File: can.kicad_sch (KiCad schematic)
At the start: 7 parts, among them U2 MCP2517FD-xJHA, U6 MCP2542FDxMF, Y1 40MHz

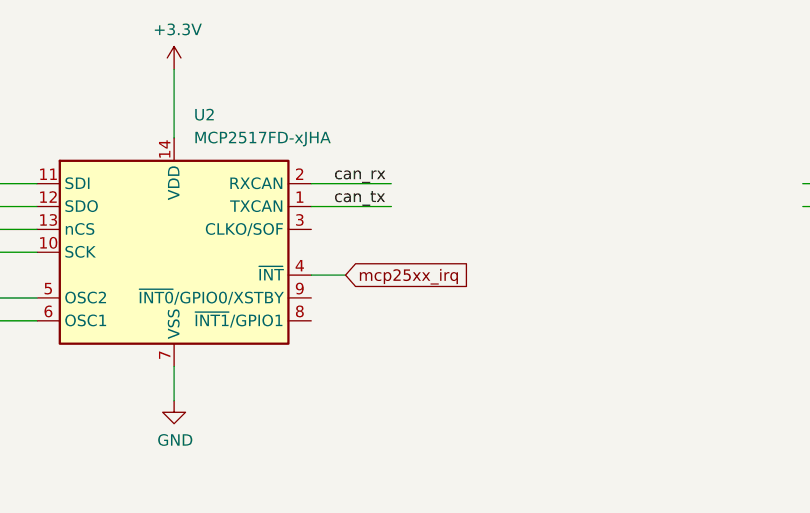
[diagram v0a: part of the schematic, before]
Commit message: move to 4 layers
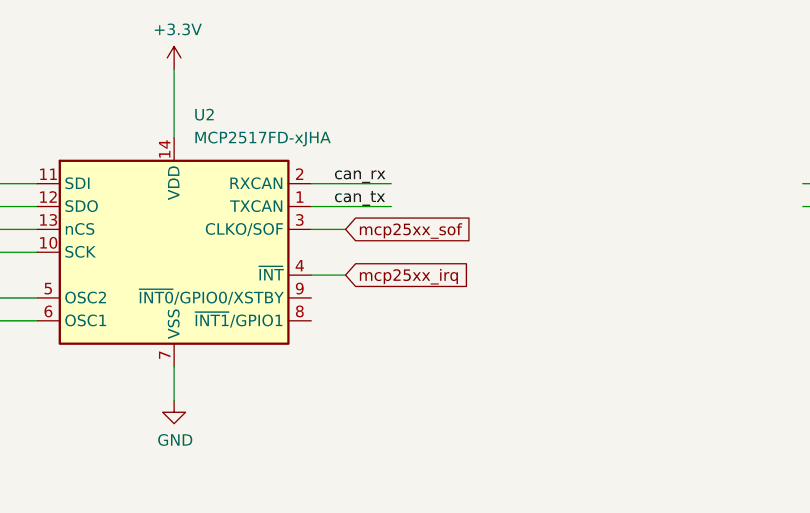
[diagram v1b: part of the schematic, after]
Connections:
- net mcp25xx_sof: now reaches U2.3 (CLKO/SOF)
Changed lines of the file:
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@@
+    (stroke (width 0) (type default))
+  )
+  (wire (pts (xy 123.19 68.58) (xy 127 68.58))
     (stroke (width 0) (type default))
   )
@@
       (effects (font (size 1.27 1.27)) hide)
     )
+  )
+  (global_label "mcp25xx_sof" (shape input) (at 127 68.58 0)
+    (effects (font (size 1.27 1.27)) (justify left))
+    (property "Intersheetrefs" "${INTERSHEET_REFS}" (at 127 68.58 0)
+      (effects (font (size 1.27 1.27)) hide)
+    )

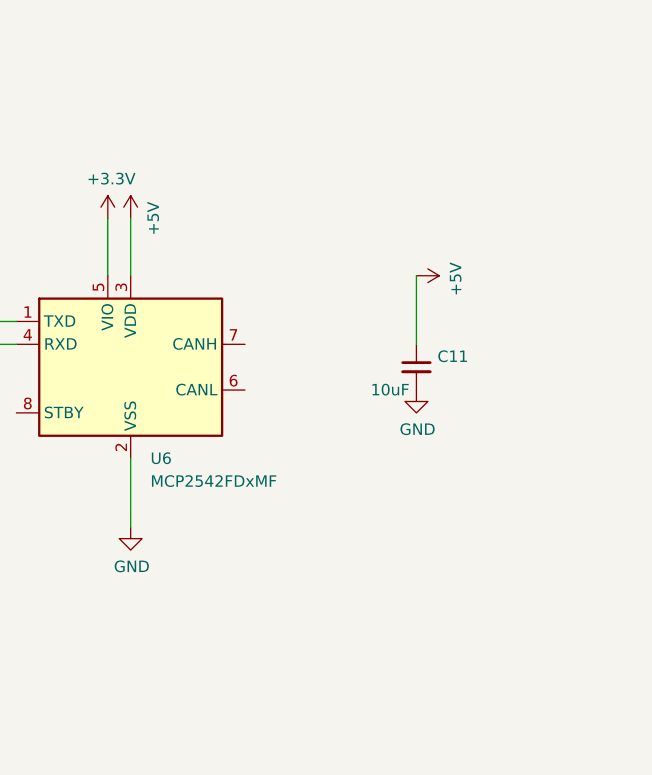
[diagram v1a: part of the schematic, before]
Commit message: Add CAN TVS protection
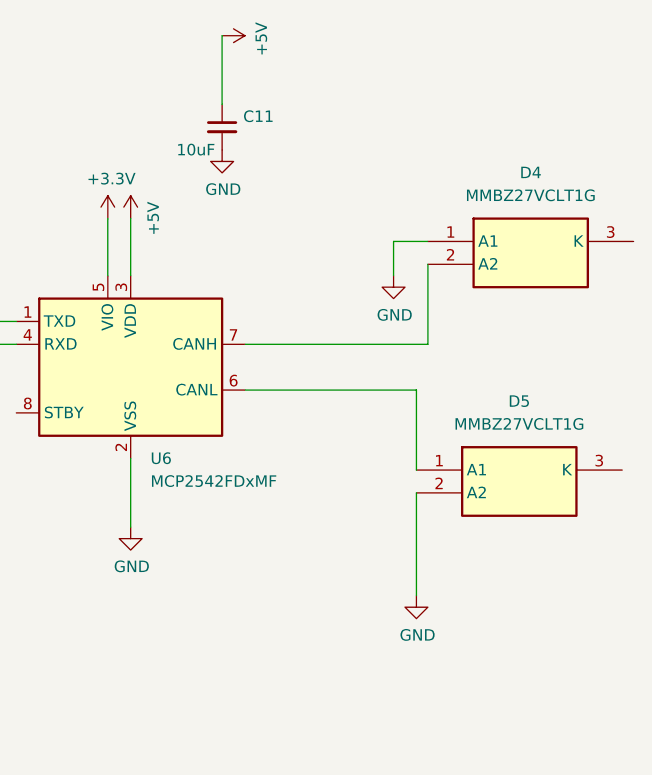
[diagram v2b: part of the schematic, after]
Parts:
- added D4, D5: MMBZ27VCLT1G, LTP-305G:SOT96P237X111-3N, symbol MMBZ27VCLT1G:MMBZ27VCLT1G
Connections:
- net GND: now also D4.1 (A1), D5.2 (A2)
- net at U6.6 (CANL): now also D5.1 (A1)
- net at U6.7 (CANH): now also D4.2 (A2)
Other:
- moved on the sheet: C11

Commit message: Add CAN stby
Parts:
- added C11: 10uF, Capacitor_SMD:C_0402_1005Metric, symbol Device:C_Small
- added J3: Conn_01x02_Pin, Connector_PinHeader_1.27mm:PinHeader_1x02_P1.27mm_Vertical, symbol Connector:Conn_01x02_Pin
- added JP1, JP2: Jumper_3_Open, Jumper:SolderJumper-3_P1.3mm_Open_RoundedPad1.0x1.5mm, symbol Jumper:Jumper_3_Open
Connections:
- net +3V3: now also C11.1
- net GND: now also C11.2
- net at D5.1 (A1), U6.6 (CANL): now also J3.1 (Pin_1)
- net at D4.2 (A2), U6.7 (CANH): now also J3.2 (Pin_2)
- net at U6.8 (STBY): now also JP2.2 (C)
- net at U2.9 (~{INT0}/GPIO0/XSTBY): now also JP1.3 (B)
- new net: JP1.2 (C), JP2.3 (B)
- new net can_stby: JP1.1 (A)

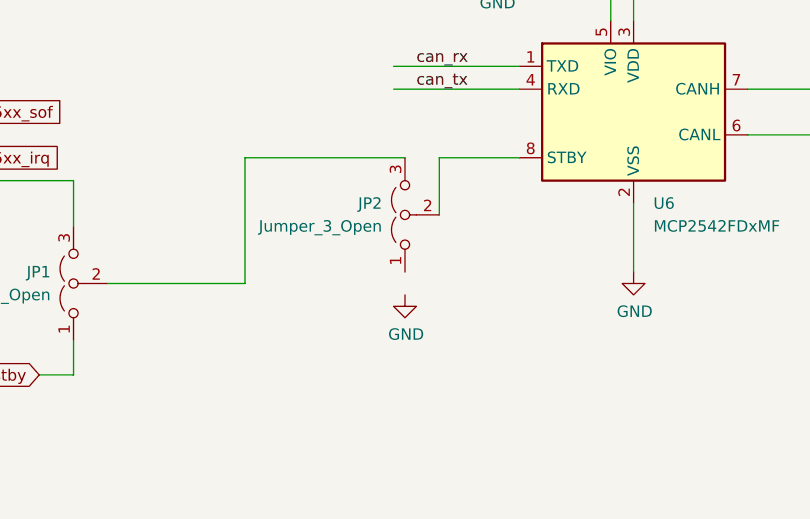
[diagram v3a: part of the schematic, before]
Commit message: Fix can stby jumper
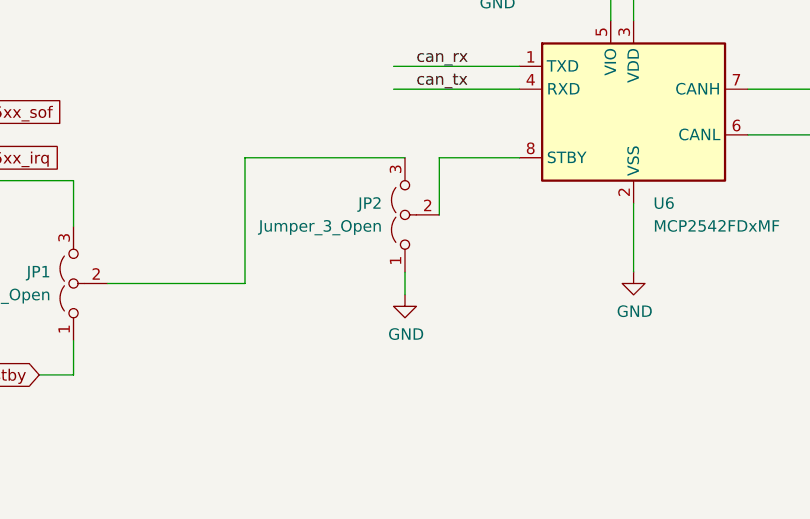
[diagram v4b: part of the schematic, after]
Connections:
- net GND: now also JP2.1 (A)
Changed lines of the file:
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@@
+    (stroke (width 0) (type default))
+  )
+  (wire (pts (xy 179.07 86.36) (xy 179.07 88.9))
     (stroke (width 0) (type default))
   )

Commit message: Verssion 0.11
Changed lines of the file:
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@@
+    (stroke (width 0) (type default))
+  )
+  (wire (pts (xy 39.37 121.92) (xy 39.37 129.54))
     (stroke (width 0) (type default))
   )
@@
         (path "/eed35b77-cbf9-4596-9b17-2558f81058ba/016e13d7-1a1a-4980-89bb-e5d4ebfcb8b8"
           (reference "#PWR099") (unit 1)
+        )
+      )
+    )
+  )
+  (symbol (lib_id "rpi-pico-debugger-shoe-rescue:+3.3V-power") (at 54.61 121.92 0) (unit 1)
+    (in_bom yes) (on_board yes) (dnp no)
+    (property "Reference" "#PWR01" (at 54.61 125.73 0)
+      (effects (font (size 1.27 1.27)) hide)
+    )
+    (property "Value" "+3.3V" (at 54.991 117.5258 0)
+      (effects (font (size 1.27 1.27)))
+    )
+    (property "Footprint" "" (at 54.61 121.92 0)
+      (effects (font (size 1.27 1.27)) hide)
+    )
+    (property "Datasheet" "" (at 54.61 121.92 0)
+      (effects (font (size 1.27 1.27)) hide)
+    )
+    (pin "1")
+    (instances
+      (project "rpi-pico-debugger-shoe"
+        (path "/aad74d97-f116-4a83-b498-c8cb2f4b4e35"
+          (reference "#PWR01") (unit 1)
+        )
+      )
+      (project "ltp_kikad"
+        (path "/eed35b77-cbf9-4596-9b17-2558f81058ba/643f5372-7b7f-4a0a-9eb8-fe959bdc465c"
+          (reference "#PWR043") (unit 1)
+        )
+        (path "/eed35b77-cbf9-4596-9b17-2558f81058ba/016e13d7-1a1a-4980-89bb-e5d4ebfcb8b8"
+          (reference "#PWR0118") (unit 1)
         )
       )
@@
         )
       )
+    )
+  )
+  (symbol (lib_id "rpi-pico-debugger-shoe-rescue:+3.3V-power") (at 39.37 121.92 0) (unit 1)
+    (in_bom yes) (on_board yes) (dnp no)
+    (property "Reference" "#PWR0104" (at 39.37 125.73 0)
+      (effects (font (size 1.27 1.27)) hide)
+    )
+    (property "Value" "+3.3V" (at 39.751 117.5258 0)
+      (effects (font (size 1.27 1.27)))
+    )
+    (property "Footprint" "" (at 39.37 121.92 0)
+      (effects (font (size 1.27 1.27)) hide)
+    )
+    (property "Datasheet" "" (at 39.37 121.92 0)
+      (effects (font (size 1.27 1.27)) hide)
+    )
+    (pin "1")
+    (instances
+      (project "rpi-pico-debugger-shoe"
+        (path "/aad74d97-f116-4a83-b498-c8cb2f4b4e35"
+          (reference "#PWR0104") (unit 1)
+        )
+      )
+      (project "ltp_kikad"
+        (path "/eed35b77-cbf9-4596-9b17-2558f81058ba/643f5372-7b7f-4a0a-9eb8-fe959bdc465c"
+          (reference "#PWR056") (unit 1)
+        )
+        (path "/eed35b77-cbf9-4596-9b17-2558f81058ba/016e13d7-1a1a-4980-89bb-e5d4ebfcb8b8"
+          (reference "#PWR0117") (unit 1)
+        )
+      )
